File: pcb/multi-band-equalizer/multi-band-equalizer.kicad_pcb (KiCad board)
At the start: 2 copper layers, 147 parts, among them J1 TagConnect_TC2030, J2 Barrel_Jack_Switch, Q1 SI2347DS-T1-BE3, U1 CS4272, U10 NE5532, U2 STM32H7B0VBTx, U3 SPX3819M5-L-3-3, U4 SPX3819M5-L-5-0, U5 NE5532, U6 NE5532, U7 NE5532, U8 NE5532, U9 NE5532

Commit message: Update schematic
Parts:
- added C1: 2u2, Capacitor_SMD:C_0805_2012Metric, F.Cu at (158.7, 129.3)
- added C10: 100n, Capacitor_SMD:C_0805_2012Metric, F.Cu at (163.1, 138.3)
- added C19: 2u2, Capacitor_SMD:C_0805_2012Metric, F.Cu at (163.1, 141.3)
- added C2: 100n, Capacitor_SMD:C_0805_2012Metric, F.Cu at (158.7, 132.3)
- added C27: C, Capacitor_SMD:C_0805_2012Metric, F.Cu at (163.1, 144.3)
- added C3: 100n, Capacitor_SMD:C_0805_2012Metric, F.Cu at (158.7, 135.3)
- added C30: C, Capacitor_SMD:C_0805_2012Metric, F.Cu at (167.6, 129.3)
- added C34: 100n, Capacitor_SMD:C_0805_2012Metric, F.Cu at (167.6, 132.3)
- added C35: 100n, Capacitor_SMD:C_0805_2012Metric, F.Cu at (167.6, 135.3)
- added C36: 100n, Capacitor_SMD:C_0805_2012Metric, F.Cu at (167.6, 138.3)
- added C37: 100n, Capacitor_SMD:C_0805_2012Metric, F.Cu at (167.6, 141.3)
- added C38: 100n, Capacitor_SMD:C_0805_2012Metric, F.Cu at (167.6, 144.3)
- added C39: 100n, Capacitor_SMD:C_0805_2012Metric, F.Cu at (172.0, 129.3)
- added C4: 100n, Capacitor_SMD:C_0805_2012Metric, F.Cu at (158.7, 138.3)
- added C40: 100n, Capacitor_SMD:C_0805_2012Metric, F.Cu at (172.0, 132.3)
- added C41: 100n, Capacitor_SMD:C_0805_2012Metric, F.Cu at (172.0, 135.3)
- added C5: 100n, Capacitor_SMD:C_0805_2012Metric, F.Cu at (158.7, 141.3)
- added C6: 100n, Capacitor_SMD:C_0805_2012Metric, F.Cu at (158.7, 144.3)
- added C7: 100n, Capacitor_SMD:C_0805_2012Metric, F.Cu at (163.1, 129.3)
- added C78: 2u2, Capacitor_SMD:C_0805_2012Metric, F.Cu at (172.0, 138.3)
- added C79: 2u2, Capacitor_SMD:C_0805_2012Metric, F.Cu at (172.0, 141.3)
- added C8: 100n, Capacitor_SMD:C_0805_2012Metric, F.Cu at (163.1, 132.3)
- added C9: 100n, Capacitor_SMD:C_0805_2012Metric, F.Cu at (163.1, 135.3)
- added FB1: 120R, Inductor_SMD:L_0805_2012Metric, F.Cu at (176.5, 146.8)
- added R14: 2k2, Resistor_SMD:R_0805_2012Metric, F.Cu at (176.4, 135.2)
- added R16: 1M, Resistor_SMD:R_0805_2012Metric, F.Cu at (176.4, 138.1)
- added R17: 1M, Resistor_SMD:R_0805_2012Metric, F.Cu at (176.4, 141.1)
- added R18: 1M, Resistor_SMD:R_0805_2012Metric, F.Cu at (176.4, 144.0)
- added R19: 1M, Resistor_SMD:R_0805_2012Metric, F.Cu at (180.8, 129.2)
- added R20: 5k1, Resistor_SMD:R_0805_2012Metric, F.Cu at (180.8, 132.2)
- added R21: 5k1, Resistor_SMD:R_0805_2012Metric, F.Cu at (180.8, 135.2)
- added R22: 5k1, Resistor_SMD:R_0805_2012Metric, F.Cu at (180.8, 138.1)
- added R23: 5k1, Resistor_SMD:R_0805_2012Metric, F.Cu at (180.8, 141.1)
- added R24: 5k1, Resistor_SMD:R_0805_2012Metric, F.Cu at (180.8, 144.0)
- added R25: 5k1, Resistor_SMD:R_0805_2012Metric, F.Cu at (185.2, 129.2)
- added R26: 5k1, Resistor_SMD:R_0805_2012Metric, F.Cu at (185.2, 132.2)
- added R27: 5k1, Resistor_SMD:R_0805_2012Metric, F.Cu at (185.2, 135.2)
- added R6: 22R, Resistor_SMD:R_0805_2012Metric, F.Cu at (176.4, 129.2)
- added R8: 5k1, Resistor_SMD:R_0805_2012Metric, F.Cu at (176.4, 132.2)
- added TP1: TestPoint, TestPoint:TestPoint_THTPad_D2.0mm_Drill1.0mm, F.Cu at (141.8, 143.7)
- renumbered C1 to C11, C2 to C12, C3 to C13, C7 to C14, C8 to C15, C4 to C16, C5 to C17, C6 to C18, C9 to C20, C10 to C21, C11 to C22, C12 to C23, C15 to C24, C16 to C25, C17 to C26, C13 to C28, C14 to C29, C18 to C31, C19 to C32, C20 to C33, C21 to C42, C22 to C43, C23 to C44, C24 to C45, C25 to C46, C26 to C47, C27 to C48, C28 to C49, C29 to C50, C30 to C51, C31 to C52, C32 to C53, C33 to C54, C34 to C55, C35 to C56, C36 to C57, C37 to C58, C38 to C59, C39 to C60, C40 to C61, C41 to C62, C42 to C63, C43 to C64, C44 to C65, C45 to C66, C46 to C67, C47 to C68, C48 to C69, C49 to C70, C50 to C71, C51 to C72, C52 to C73, C53 to C74, C54 to C75, C55 to C76, C56 to C77, D5 to D6, D6 to D7, D7 to D8, FB1 to FB2, R9 to R10, R7 to R11, R10 to R12, R11 to R13, R12 to R15, R13 to R28, R14 to R29, R15 to R30, R16 to R31, R17 to R32, R18 to R33, R19 to R34, R20 to R35, R21 to R36, R22 to R37, R23 to R38, R24 to R39, R25 to R40, R26 to R41, R27 to R42, R28 to R43, R29 to R44, R30 to R45, R31 to R46, R32 to R47, R33 to R48, R34 to R49, R35 to R50, R36 to R51, R37 to R52, R38 to R53, R39 to R54, R40 to R55, R41 to R56, R42 to R57, R43 to R58, R44 to R59, R45 to R60, R46 to R61, R47 to R62, R48 to R63, R49 to R64, R50 to R65, R51 to R66, R52 to R67, R53 to R68, R54 to R69, R6 to R7, R55 to R70, R56 to R71, R57 to R72, R58 to R73, R59 to R74, R60 to R75, R61 to R76, R62 to R77, R63 to R78, R64 to R79, R65 to R80, R66 to R81, R8 to R9
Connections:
- net /ASIGNAL_OUT_L renamed /CODEC_AOUT_L
- net /ASIGNAL_OUT_R renamed /CODEC_AOUT_R
- D6 pad 1: unconnected-(D5-K-Pad1) -> Net-(D6-K)
- D6 pad 2: unconnected-(D5-A-Pad2) -> /MCU_LED_STATUS_RED
- R11 pad 1: /CODEC_NRST -> /CODEC_NRST_FILT
- R13 pad 1: /I2S_OUT -> /I2S_SDO
- U1 pad 14: /CODEC_NRST -> /CODEC_NRST_FILT
- U1 pad 6: /I2S_OUT -> /I2S_SDO
- U1 pad 7: /I2S_IN -> /I2S_SDI
- U2 pad 100: unconnected-(U2-VDD-Pad100) -> +3.3V
- U2 pad 11: unconnected-(U2-VDD-Pad11) -> +3.3V
- U2 pad 12: unconnected-(U2-PH0-Pad12) -> /MCU_XTI
- U2 pad 13: unconnected-(U2-PH1-Pad13) -> Net-(U2-PH1)
- U2 pad 20: +3.3V -> /VDDA
- U2 pad 21: unconnected-(U2-VDDA-Pad21) -> /VDDA
- U2 pad 27: unconnected-(U2-VDD-Pad27) -> +3.3V
- U2 pad 28: unconnected-(U2-PA4-Pad28) -> /CTRL_KNB_100_HZ
- U2 pad 29: unconnected-(U2-PA5-Pad29) -> /CTRL_KNB_200_HZ
- U2 pad 30: unconnected-(U2-PA6-Pad30) -> /CTRL_KNB_400_HZ
- U2 pad 31: unconnected-(U2-PA7-Pad31) -> /CTRL_KNB_800_HZ
- U2 pad 32: unconnected-(U2-PC4-Pad32) -> /CTRL_KNB_1600_HZ
- U2 pad 33: unconnected-(U2-PC5-Pad33) -> /CTRL_KNB_3200_HZ
- U2 pad 34: unconnected-(U2-PB0-Pad34) -> /CTRL_KNB_6400_HZ
- U2 pad 35: unconnected-(U2-PB1-Pad35) -> /CTRL_KNB_VOL_LVL
- U2 pad 45: unconnected-(U2-PE15-Pad45) -> /MCU_LED_STATUS_RED
- U2 pad 48: unconnected-(U2-VCAP-Pad48) -> Net-(C78-Pad1)
- U2 pad 50: unconnected-(U2-VDD-Pad50) -> +3.3V
- U2 pad 51: unconnected-(U2-PB12-Pad51) -> /I2S_LRCK
- U2 pad 52: unconnected-(U2-PB13-Pad52) -> /I2S_SCLK
- U2 pad 53: unconnected-(U2-PB14-Pad53) -> /I2S_SDI
- U2 pad 54: unconnected-(U2-PB15-Pad54) -> /I2S_SDO
- U2 pad 6: unconnected-(U2-VBAT-Pad6) -> +3.3V
- U2 pad 63: unconnected-(U2-PC6-Pad63) -> /I2S_MCLK
- U2 pad 72: unconnected-(U2-PA13-Pad72) -> /MCU_SWDIO
- U2 pad 73: unconnected-(U2-VCAP-Pad73) -> Net-(C79-Pad1)
- U2 pad 75: unconnected-(U2-VDD-Pad75) -> +3.3V
- U2 pad 76: unconnected-(U2-PA14-Pad76) -> /MCU_SWCLK
- U2 pad 80: unconnected-(U2-PC12-Pad80) -> /CODEC_NRST
- U2 pad 89: unconnected-(U2-PB3-Pad89) -> /MCU_SWO
- U2 pad 92: unconnected-(U2-PB6-Pad92) -> /I2C_SCL
- U2 pad 93: unconnected-(U2-PB7-Pad93) -> /I2C_SDA

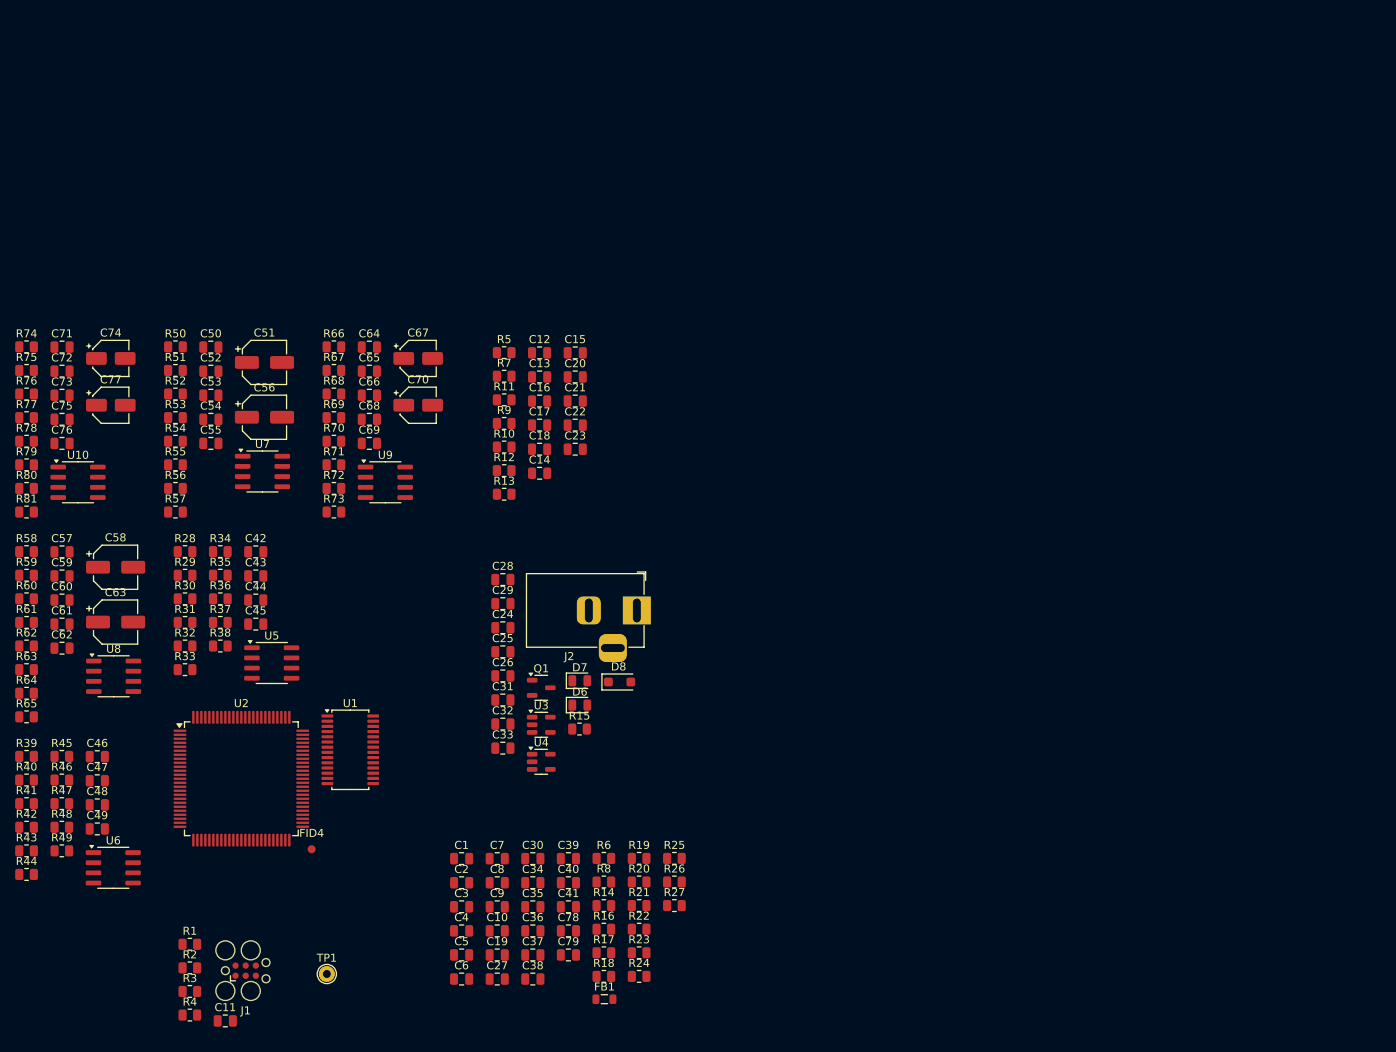
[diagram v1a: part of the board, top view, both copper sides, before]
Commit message: sliding potentiometers
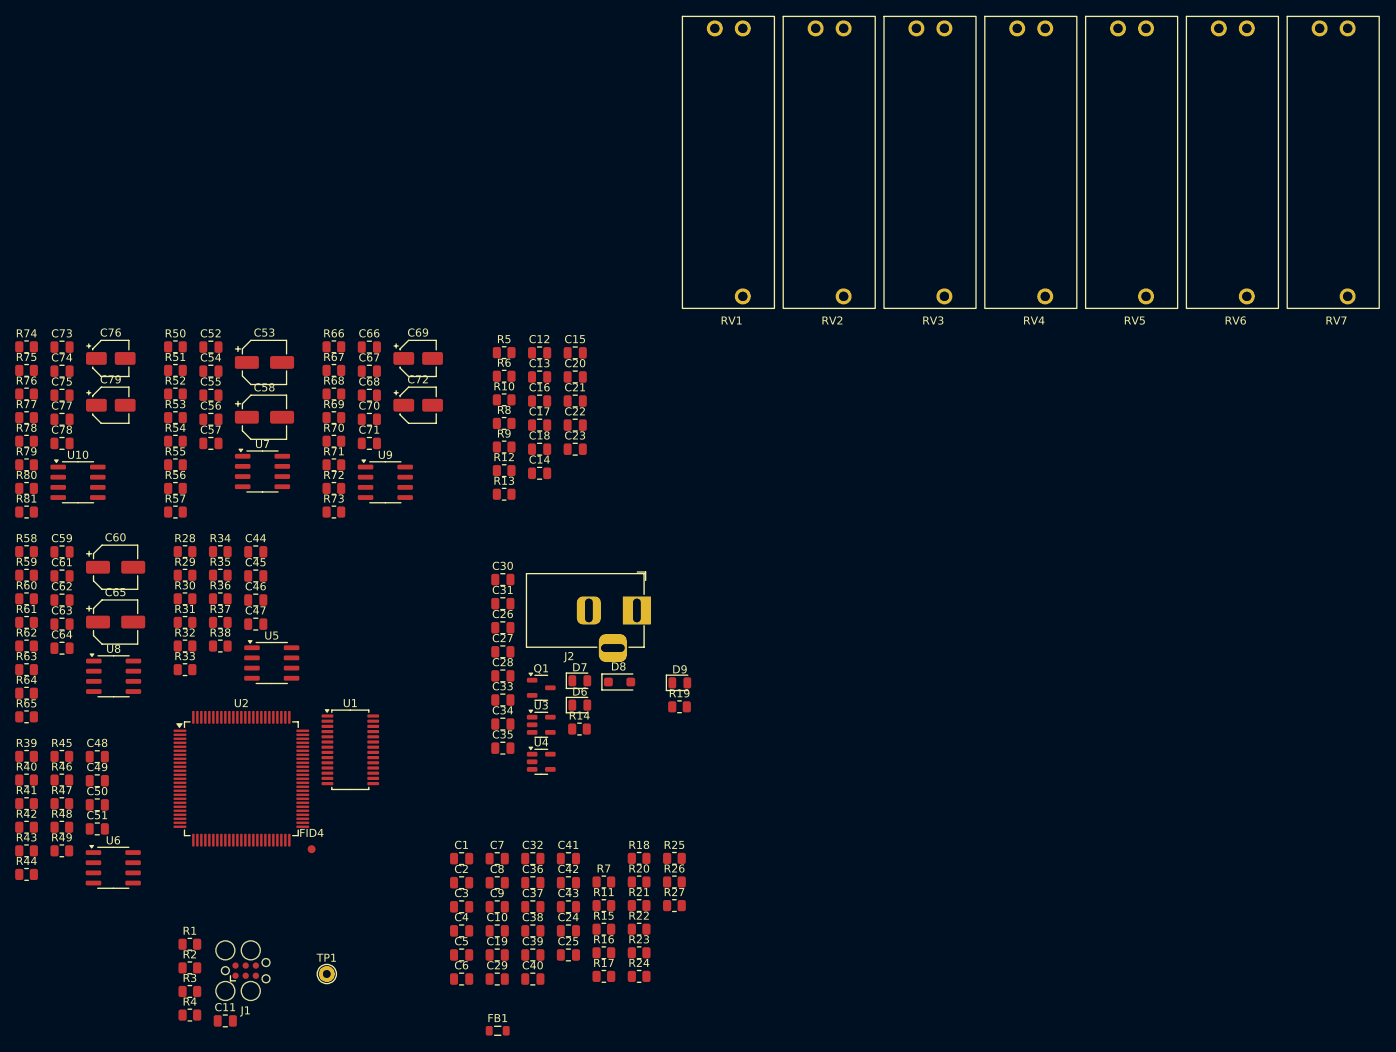
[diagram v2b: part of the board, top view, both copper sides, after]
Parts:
- removed the R6 at (176.4, 129.2)
- added D9: LED_GREEN, LED_SMD:LED_0805_2012Metric, F.Cu at (185.9, 107.3)
- added R19: 2k2, Resistor_SMD:R_0805_2012Metric, F.Cu at (185.9, 110.3)
- added RV1: 5k, Custom_Potentiometers:PTA2043-2015CPB502, F.Cu at (193.8, 59.0)
- added RV2: 5k, Custom_Potentiometers:PTA2043-2015CPB502, F.Cu at (206.4, 59.0)
- added RV3: 5k, Custom_Potentiometers:PTA2043-2015CPB502, F.Cu at (219.0, 59.0)
- added RV4: 5k, Custom_Potentiometers:PTA2043-2015CPB502, F.Cu at (231.6, 59.0)
- added RV5: 5k, Custom_Potentiometers:PTA2043-2015CPB502, F.Cu at (244.2, 59.0)
- added RV6: 5k, Custom_Potentiometers:PTA2043-2015CPB502, F.Cu at (256.8, 59.0)
- added RV7: 5k, Custom_Potentiometers:PTA2043-2015CPB502, F.Cu at (269.4, 59.0)
- C10, C9: value 100n -> 2u2
- moved FB1 13.9 mm to (163.2, 150.8)
- renumbered C78 to C24, C79 to C25, C24 to C26, C25 to C27, C26 to C28, C27 to C29, C28 to C30, C29 to C31, C30 to C32, C31 to C33, C32 to C34, C33 to C35, C34 to C36, C35 to C37, C36 to C38, C37 to C39, C38 to C40, C39 to C41, C40 to C42, C41 to C43, C42 to C44, C43 to C45, C44 to C46, C45 to C47, C46 to C48, C47 to C49, C48 to C50, C49 to C51, C50 to C52, C51 to C53, C52 to C54, C53 to C55, C54 to C56, C55 to C57, C56 to C58, C57 to C59, C58 to C60, C59 to C61, C60 to C62, C61 to C63, C62 to C64, C63 to C65, C64 to C66, C65 to C67, C66 to C68, C67 to C69, C68 to C70, C69 to C71, C70 to C72, C71 to C73, C72 to C74, C73 to C75, C74 to C76, C75 to C77, C76 to C78, C77 to C79, R11 to R10, R14 to R11, R15 to R14, R16 to R15, R17 to R16, R18 to R17, R19 to R18, R7 to R6, R8 to R7, R9 to R8, R10 to R9
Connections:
- U2 pad 13: Net-(U2-PH1) -> /MCU_XTO
- U2 pad 66: unconnected-(U2-PC9-Pad66) -> /I2C_SDA
- U2 pad 67: unconnected-(U2-PA8-Pad67) -> /I2C_SCL
- U2 pad 69: unconnected-(U2-PA10-Pad69) -> /CODEC_NRST
- U2 pad 80: /CODEC_NRST -> unconnected-(U2-PC12-Pad80)
- U2 pad 92: /I2C_SCL -> unconnected-(U2-PB6-Pad92)
- U2 pad 93: /I2C_SDA -> unconnected-(U2-PB7-Pad93)

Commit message: Update pcb
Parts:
- removed the C16 at (168.4, 72.1)
- removed the C29 at (163.1, 144.3)
- removed the C32 at (167.6, 129.3)
- removed the R18 at (180.8, 129.2)
- removed the R5 at (164.0, 66.0)
- added C30: 10p, Capacitor_SMD:C_0805_2012Metric, F.Cu at (152.6, 317.6)
- added C31: 10p, Capacitor_SMD:C_0805_2012Metric, F.Cu at (152.6, 321.5)
- added D1: Zener, Diode_SMD:D_SOD-323, F.Cu at (188.0, 368.6)
- added D2: Zener, Diode_SMD:D_SOD-323, F.Cu at (188.0, 371.6)
- added D3: Zener, Diode_SMD:D_SOD-323, F.Cu at (188.0, 374.5)
- added D4: Zener, Diode_SMD:D_SOD-323, F.Cu at (188.0, 377.5)
- added D5: Zener, Diode_SMD:D_SOD-323, F.Cu at (188.0, 380.4)
- added R14: 1M, Resistor_SMD:R_0805_2012Metric, F.Cu at (305.7, 353.1)
- added S1: SF12011F-0202-20R-M-050, Custom_Switches:SF12011F020220RM050, F.Cu at (290.0, 359.0)
- added SW1: SW_Push, Button_Switch_THT:SW_PUSH_6mm_H4.3mm, F.Cu at (170.2, 280.9)
- added TP10: TestPoint, TestPoint:TestPoint_THTPad_D1.0mm_Drill0.5mm, F.Cu at (176.6, 294.3)
- added TP11: TestPoint, TestPoint:TestPoint_THTPad_D1.0mm_Drill0.5mm, F.Cu at (176.6, 297.4)
- added TP12: TestPoint, TestPoint:TestPoint_THTPad_D1.0mm_Drill0.5mm, F.Cu at (90.5, 372.2)
- added TP13: TestPoint, TestPoint:TestPoint_THTPad_D1.0mm_Drill0.5mm, F.Cu at (368.2, 291.9)
- added TP14: TestPoint, TestPoint:TestPoint_THTPad_D1.0mm_Drill0.5mm, F.Cu at (368.2, 295.0)
- added TP15: TestPoint, TestPoint:TestPoint_THTPad_D1.0mm_Drill0.5mm, F.Cu at (368.2, 298.1)
- added TP16: TestPoint, TestPoint:TestPoint_THTPad_D1.0mm_Drill0.5mm, F.Cu at (368.2, 301.1)
- added TP17: TestPoint, TestPoint:TestPoint_THTPad_D1.0mm_Drill0.5mm, F.Cu at (371.3, 291.9)
- added TP18: TestPoint, TestPoint:TestPoint_THTPad_D1.0mm_Drill0.5mm, F.Cu at (371.3, 295.0)
- added TP19: TestPoint, TestPoint:TestPoint_THTPad_D1.0mm_Drill0.5mm, F.Cu at (371.3, 298.1)
- added TP2: TestPoint, TestPoint:TestPoint_THTPad_D1.0mm_Drill0.5mm, F.Cu at (170.5, 294.3)
- added TP20: TestPoint, TestPoint:TestPoint_THTPad_D1.0mm_Drill0.5mm, F.Cu at (371.3, 301.1)
- added TP3: TestPoint, TestPoint:TestPoint_THTPad_D1.0mm_Drill0.5mm, F.Cu at (170.5, 297.4)
- added TP4: TestPoint, TestPoint:TestPoint_THTPad_D1.0mm_Drill0.5mm, F.Cu at (170.5, 300.4)
- added TP5: TestPoint, TestPoint:TestPoint_THTPad_D1.0mm_Drill0.5mm, F.Cu at (173.6, 291.2)
- added TP6: TestPoint, TestPoint:TestPoint_THTPad_D1.0mm_Drill0.5mm, F.Cu at (173.6, 294.3)
- added TP7: TestPoint, TestPoint:TestPoint_THTPad_D1.0mm_Drill0.5mm, F.Cu at (173.6, 297.4)
- added TP8: TestPoint, TestPoint:TestPoint_THTPad_D1.0mm_Drill0.5mm, F.Cu at (173.6, 300.4)
- added TP9: TestPoint, TestPoint:TestPoint_THTPad_D1.0mm_Drill0.5mm, F.Cu at (176.6, 291.2)
- added Y1: 24 MHz, Crystal:Crystal_SMD_2520-4Pin_2.5x2.0mm, F.Cu at (149.4, 319.6)
- TP1: footprint TestPoint:TestPoint_THTPad_D2.0mm_Drill1.0mm -> TestPoint:TestPoint_THTPad_D1.0mm_Drill0.5mm
- moved FB2 299.5 mm to (83.4, 372.2)
- moved C25 273.2 mm to (67.8, 356.2)
- moved C26 273.2 mm to (67.8, 359.2)
- moved C27 273.2 mm to (67.8, 362.2)
- moved C32 273.2 mm to (67.8, 365.2)
- moved C33 273.2 mm to (67.8, 368.2)
- moved D7 273.2 mm to (77.4, 362.8)
- moved D8 273.2 mm to (82.3, 363.0)
- moved D9 273.2 mm to (89.9, 363.1)
- moved J2 273.2 mm to (84.5, 354.0)
- moved R13 273.2 mm to (77.3, 368.9)
- moved C28 273.2 mm to (67.8, 350.2)
- moved C29 273.2 mm to (67.8, 353.2)
- moved C34 273.2 mm to (67.8, 371.3)
- moved Q1 273.2 mm to (72.5, 363.7)
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- renumbered C17 to C16, C18 to C17, C19 to C18, C20 to C19, C21 to C20, C22 to C21, C23 to C22, C24 to C23, C25 to C24, C26 to C25, C27 to C26, C28 to C27, C30 to C28, C31 to C29, C33 to C32, C34 to C33, C35 to C34, C36 to C35, C37 to C36, C38 to C37, C39 to C38, C40 to C39, C41 to C40, C42 to C41, C43 to C42, C44 to C43, C45 to C44, C46 to C45, C47 to C46, C48 to C47, C49 to C48, C50 to C49, C51 to C50, C52 to C51, C53 to C52, C54 to C53, C55 to C54, C56 to C55, C57 to C56, C58 to C57, C59 to C58, C60 to C59, C61 to C60, C62 to C61, C63 to C62, C64 to C63, C65 to C64, C66 to C65, C67 to C66, C68 to C67, C69 to C68, C70 to C69, C71 to C70, C72 to C71, C73 to C72, C74 to C73, C75 to C74, C76 to C75, C77 to C76, C78 to C77, C79 to C78, R11 to R10, R12 to R11, R13 to R12, R14 to R13, R19 to R18, R20 to R19, R21 to R20, R22 to R21, R23 to R22, R24 to R23, R25 to R24, R26 to R25, R27 to R26, R28 to R27, R29 to R28, R30 to R29, R31 to R30, R32 to R31, R33 to R32, R34 to R33, R35 to R34, R36 to R35, R37 to R36, R38 to R37, R39 to R38, R40 to R39, R41 to R40, R42 to R41, R43 to R42, R44 to R43, R45 to R44, R46 to R45, R47 to R46, R48 to R47, R49 to R48, R50 to R49, R6 to R5, R51 to R50, R52 to R51, R53 to R52, R54 to R53, R55 to R54, R56 to R55, R57 to R56, R58 to R57, R59 to R58, R60 to R59, R7 to R6, R61 to R60, R62 to R61, R63 to R62, R64 to R63, R65 to R64, R66 to R65, R67 to R66, R68 to R67, R69 to R68, R70 to R69, R8 to R7, R71 to R70, R72 to R71, R73 to R72, R74 to R73, R75 to R74, R76 to R75, R77 to R76, R78 to R77, R79 to R78, R80 to R79, R9 to R8, R81 to R80, R10 to R9
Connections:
- R15 pad 1: /ASIGNAL_IN_R -> /ASIGNAL_IN_L
- R16 pad 1: /CODEC_AOUT_R -> /ASIGNAL_IN_R
- R17 pad 1: /ASIGNAL_IN_L -> /CODEC_AOUT_R
- TP1 pad 1: unconnected-(TP1-Pad1) -> +3.3V
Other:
- copper layers 2 -> 4

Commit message: Updated pcb and script
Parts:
- removed the C42 at (332.1, 296.6)
- removed the R26 at (345.3, 296.4)
- removed the TP20 at (371.3, 301.1)
- removed the TP5 at (173.6, 291.2)
- added C36: 100n, Capacitor_SMD:C_0805_2012Metric, F.Cu at (261.4, 198.6)
- added C37: 100n, Capacitor_SMD:C_0805_2012Metric, F.Cu at (279.3, 198.0)
- added C44: 100n, Capacitor_SMD:C_0805_2012Metric, F.Cu at (407.2, 198.5)
- added C45: 100n, Capacitor_SMD:C_0805_2012Metric, F.Cu at (428.4, 198.3)
- added R20: 5k1, Resistor_SMD:R_0805_2012Metric, F.Cu at (261.4, 201.6)
- added R21: 5k1, Resistor_SMD:R_0805_2012Metric, F.Cu at (279.3, 200.9)
- added R28: 5k1, Resistor_SMD:R_0805_2012Metric, F.Cu at (407.2, 201.4)
- added R29: 5k1, Resistor_SMD:R_0805_2012Metric, F.Cu at (428.4, 201.3)
- added RV10: 5k, Custom_Potentiometers:PTA2043-2015CPB502, F.Cu at (410.2, 192.2)
- added RV11: 5k, Custom_Potentiometers:PTA2043-2015CPB502, F.Cu at (431.0, 192.2)
- added RV2: 5k, Custom_Potentiometers:PTA2043-2015CPB502, F.Cu at (264.7, 192.2)
- added RV3: 5k, Custom_Potentiometers:PTA2043-2015CPB502, F.Cu at (283.0, 192.3)
- added TP14: TestPoint, TestPoint:TestPoint_THTPad_D1.0mm_Drill0.5mm, F.Cu at (265.2, 201.6)
- added TP15: TestPoint, TestPoint:TestPoint_THTPad_D1.0mm_Drill0.5mm, F.Cu at (283.0, 201.0)
- added TP22: TestPoint, TestPoint:TestPoint_THTPad_D1.0mm_Drill0.5mm, F.Cu at (410.9, 201.5)
- added TP23: TestPoint, TestPoint:TestPoint_THTPad_D1.0mm_Drill0.5mm, F.Cu at (432.1, 201.3)
- added TP9: TestPoint, TestPoint:TestPoint_THTPad_D1.0mm_Drill0.5mm, F.Cu at (300.4, 238.3)
- C14: value 100n -> 1u
- C15: value 1u -> 100n
- moved Q1 362.1 mm to (341.9, 121.7)
- moved R13 358.7 mm to (351.3, 137.4), turned to 90 degrees
- moved D8 357.7 mm to (341.8, 116.7)
- moved U3 356.3 mm to (343.9, 137.5), turned to -90 degrees
- moved C25 356.3 mm to (348.0, 136.2)
- moved C28 355.8 mm to (343.7, 125.6)
- moved C29 355.8 mm to (343.7, 128.6)
- moved FB2 355.4 mm to (340.7, 127.0), turned to -90 degrees
- moved J2 354.7 mm to (343.2, 111.4), turned to -90 degrees
- moved C27 352.3 mm to (340.7, 139.6), turned to -90 degrees
- moved C26 351.9 mm to (344.0, 141.2), turned to 180 degrees
- moved D7 351.5 mm to (348.0, 138.6), turned to 180 degrees
- moved C32 347.2 mm to (328.9, 136.4)
- moved U4 345.0 mm to (324.8, 137.5), turned to -90 degrees
- moved TP12 344.6 mm to (333.7, 128.1)
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- renumbered C36 to C38, C37 to C39, C38 to C40, C39 to C41, C40 to C42, C41 to C43, C43 to C46, C44 to C47, C45 to C48, C46 to C49, C47 to C50, C48 to C51, C49 to C52, C50 to C53, C51 to C54, C52 to C55, C53 to C56, C54 to C57, C55 to C58, C56 to C59, C57 to C60, C58 to C61, C59 to C62, C60 to C63, C61 to C64, C62 to C65, C63 to C66, C64 to C67, C65 to C68, C66 to C69, C67 to C70, C68 to C71, C69 to C72, C70 to C73, C71 to C74, C72 to C75, C73 to C76, C74 to C77, C75 to C78, C76 to C79, C77 to C80, C78 to C81, R20 to R22, R21 to R23, R22 to R24, R23 to R25, R24 to R26, R25 to R27, R27 to R30, R28 to R31, R29 to R32, R30 to R33, R31 to R34, R32 to R35, R33 to R36, R34 to R37, R35 to R38, R36 to R39, R37 to R40, R38 to R41, R39 to R42, R40 to R43, R41 to R44, R42 to R45, R43 to R46, R44 to R47, R45 to R48, R46 to R49, R47 to R50, R48 to R51, R49 to R52, R50 to R53, R51 to R54, R52 to R55, R53 to R56, R54 to R57, R55 to R58, R56 to R59, R57 to R60, R58 to R61, R59 to R62, R60 to R63, R61 to R64, R62 to R65, R63 to R66, R64 to R67, R65 to R68, R66 to R69, R67 to R70, R68 to R71, R69 to R72, R70 to R73, R71 to R74, R72 to R75, R73 to R76, R74 to R77, R75 to R78, R76 to R79, R77 to R80, R78 to R81, R79 to R82, R80 to R83, RV2 to RV4, RV3 to RV5, RV4 to RV6, RV5 to RV7, RV6 to RV8, RV7 to RV9, TP14 to TP16, TP15 to TP17, TP16 to TP18, TP17 to TP19, TP18 to TP20, TP19 to TP21, TP6 to TP5, TP7 to TP6, TP8 to TP7, TP9 to TP8
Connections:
- C35 pad 1: /CTRL_KNB_100_HZ -> /CTRL_KNB_30_HZ
- R19 pad 2: /CTRL_KNB_100_HZ -> /CTRL_KNB_30_HZ
- TP13 pad 1: /CTRL_KNB_100_HZ -> /CTRL_KNB_30_HZ
- U2 pad 23: unconnected-(U2-PA1-Pad23) -> /CTRL_KNB_VOL_LVL
- U2 pad 24: unconnected-(U2-PA2-Pad24) -> /CTRL_KNB_12800_HZ
- U2 pad 25: unconnected-(U2-PA3-Pad25) -> /CTRL_KNB_6400_HZ
- U2 pad 28: /CTRL_KNB_100_HZ -> /CTRL_KNB_3200_HZ
- U2 pad 29: /CTRL_KNB_200_HZ -> /CTRL_KNB_1600_HZ
- U2 pad 30: /CTRL_KNB_400_HZ -> /CTRL_KNB_800_HZ
- U2 pad 31: /CTRL_KNB_800_HZ -> /CTRL_KNB_400_HZ
- U2 pad 32: /CTRL_KNB_1600_HZ -> /CTRL_KNB_200_HZ
- U2 pad 33: /CTRL_KNB_3200_HZ -> /CTRL_KNB_120_HZ
- U2 pad 34: /CTRL_KNB_6400_HZ -> /CTRL_KNB_60_HZ
- U2 pad 35: /CTRL_KNB_VOL_LVL -> /CTRL_KNB_30_HZ
- U2 pad 56: unconnected-(U2-PD9-Pad56) -> /CODEC_NRST
- U2 pad 69: /CODEC_NRST -> unconnected-(U2-PA10-Pad69)
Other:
- board outline added: 349 x 263 mm

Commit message: update pcb
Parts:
- added J3: Input Audio, Custom_Connectors:ACJSMHDR, F.Cu at (236.2, 166.0)
- added J4: Output Audio, Custom_Connectors:ACJSMHDR, F.Cu at (497.4, 180.5)
- U2: value STM32H7B0VBTx -> STM32H7B0VBT6
- moved H1 315.3 mm to (472.6, 258.7)
- moved H2 315.3 mm to (472.6, 266.6)
- moved H3 315.3 mm to (472.6, 274.6)
- moved H4 315.3 mm to (472.6, 282.6)
- moved FID4 309.4 mm to (478.4, 270.1)
- moved FID1 308.5 mm to (478.9, 257.0)
- moved FID2 308.5 mm to (478.9, 261.6)
- moved FID3 308.5 mm to (478.9, 266.1)
- moved R72 254.6 mm to (412.4, 152.9), turned to 180 degrees
- moved R69 254.4 mm to (417.9, 152.9), turned to 0 degrees
- moved C73 251.2 mm to (410.5, 155.3), turned to 0 degrees
- moved C68 250.9 mm to (419.8, 155.2), turned to 180 degrees
- moved R68 238.6 mm to (421.0, 158.2), turned to -90 degrees
- moved R70 232.8 mm to (418.8, 158.2), turned to -90 degrees
- moved U9 232.1 mm to (416.5, 167.2), turned to -90 degrees
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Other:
- board size 349 x 263 mm -> 270.6 x 203.1 mm
